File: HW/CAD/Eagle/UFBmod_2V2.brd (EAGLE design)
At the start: 98.4 x 89.5 mm, 204 parts, among them J1411 ABRACON_ARJE-0034, T0551 MMBT2222, U0501 MIDAS_MCCOG21605B6W-FPTLWI, U0601 MAX5217, U0701 AT86RF215-ZU, U0711 ASVTX-13-D-26.000MHZ-I05-T, U0811 PE4259, U0821 RFX1010, U0881 B39871B3440U410, U0911 FT232HL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

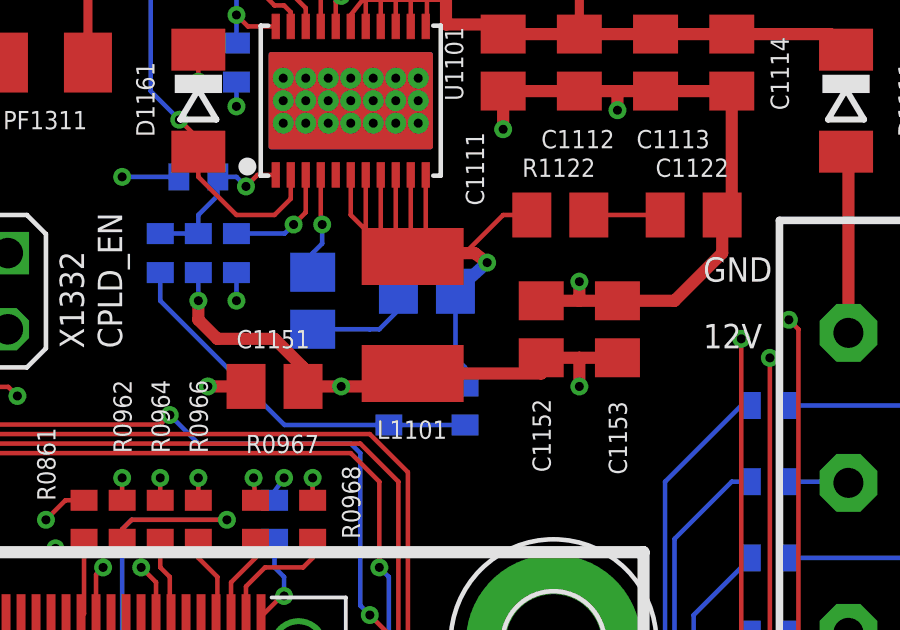
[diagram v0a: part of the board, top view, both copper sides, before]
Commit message: HW - Eagle - V2.2 - inductor sizes fixed
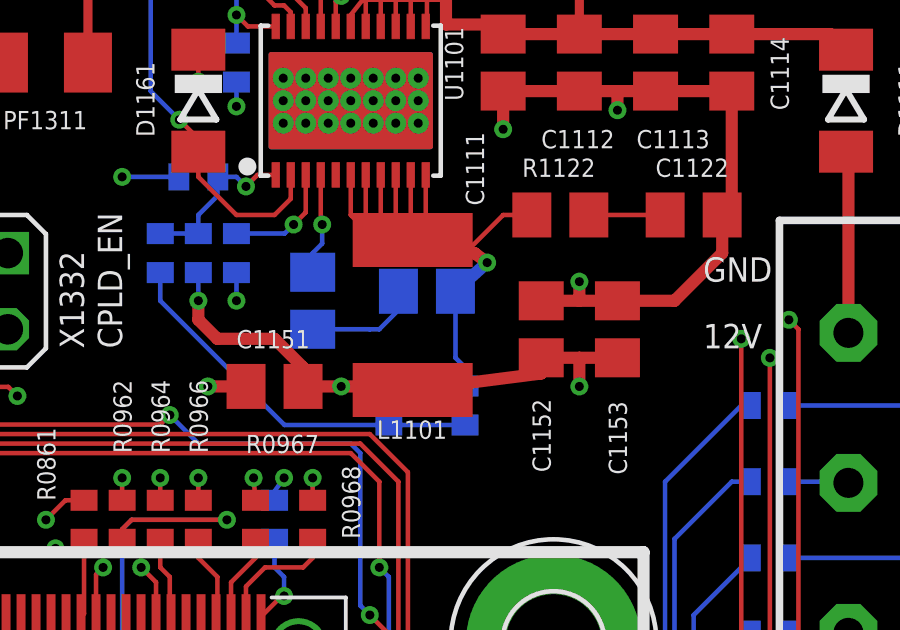
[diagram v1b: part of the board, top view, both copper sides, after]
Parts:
- L1101: value 440nH -> 470nH; device df4iah_rcl:L1812 -> df4iah_rcl:L5650M
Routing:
- net TPS_LL: track 31.4 -> 33.1 mm
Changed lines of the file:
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@@
 <layer number="42" name="bRestrict" color="1" fill="10" visible="yes" active="yes"/>
 <layer number="43" name="vRestrict" color="2" fill="10" visible="yes" active="yes"/>
-<layer number="44" name="Drills" color="7" fill="1" visible="yes" active="yes"/>
+<layer number="44" name="Drills" color="7" fill="1" visible="no" active="yes"/>
 <layer number="45" name="Holes" color="7" fill="1" visible="yes" active="yes"/>
 <layer number="46" name="Milling" color="3" fill="1" visible="yes" active="yes"/>
-<layer number="47" name="Measures" color="13" fill="1" visible="no" active="yes"/>
+<layer number="47" name="Measures" color="13" fill="1" visible="yes" active="yes"/>
 <layer number="48" name="Document" color="7" fill="1" visible="yes" active="yes"/>
 <layer number="49" name="Reference" color="7" fill="1" visible="yes" active="yes"/>
@@
 <element name="H1512" library="df4iah_holes" package="3,2-PAD" value="MOUNT-PAD-ROUND3.2" x="5.08" y="5.08" locked="yes" smashed="yes"/>
 <element name="H1514" library="df4iah_holes" package="3,2-PAD" value="MOUNT-PAD-ROUND3.2" x="93.345" y="5.08" locked="yes" smashed="yes"/>
-<element name="L1101" library="df4iah_rcl" package="L1812" value="440nH" x="73.18375" y="72.86625" smashed="yes" rot="R90">
+<element name="L1101" library="df4iah_rcl" package="L5650M" value="470nH" x="73.18375" y="72.86625" smashed="yes" rot="R90">
 <attribute name="NAME" x="71.993125" y="68.73875" size="0.6096" layer="25" font="vector" ratio="10"/>
 <attribute name="VALUE" x="75.72375" y="71.59625" size="0.6096" layer="27" font="vector" ratio="10" rot="R90"/>
@@
 <wire x1="77.47" y1="71.44" x2="78.74" y2="71.44" width="0.4064" layer="1"/>
 <wire x1="78.74" y1="71.44" x2="80.01" y2="71.44" width="0.4064" layer="1"/>
-<wire x1="73.18375" y1="70.91625" x2="77.47" y2="70.91625" width="0.4064" layer="1"/>
+<wire x1="73.18375" y1="70.36625" x2="77.47" y2="70.91625" width="0.4064" layer="1"/>
 <wire x1="77.47" y1="70.91625" x2="77.47" y2="71.44" width="0.4064" layer="1"/>
 <wire x1="69.53" y1="70.485" x2="70.8025" y2="70.485" width="0.4064" layer="1"/>
 <wire x1="70.8025" y1="70.485" x2="73.18375" y2="70.485" width="0.4064" layer="1"/>
-<wire x1="73.18375" y1="70.485" x2="73.18375" y2="70.91625" width="0.4064" layer="1"/>
+<wire x1="73.18375" y1="70.485" x2="73.18375" y2="70.36625" width="0.4064" layer="1"/>
 <via x="78.74" y="70.485" extent="1-16" drill="0.3"/>
 <wire x1="78.74" y1="70.485" x2="78.74" y2="71.44" width="0.4064" layer="1"/>
@@
 <wire x1="71.12" y1="77.535" x2="71.12" y2="76.2" width="0.1524" layer="1"/>
 <wire x1="71.12" y1="76.2" x2="72.50375" y2="74.81625" width="0.1524" layer="1"/>
-<wire x1="72.50375" y1="74.81625" x2="73.18375" y2="74.81625" width="0.1524" layer="1"/>
+<wire x1="72.50375" y1="74.81625" x2="73.18375" y2="75.36625" width="0.1524" layer="1"/>
 <wire x1="71.62" y1="77.535" x2="71.62" y2="74.81625" width="0.1524" layer="1"/>
-<wire x1="71.62" y1="74.81625" x2="73.18375" y2="74.81625" width="0.1524" layer="1"/>
+<wire x1="71.62" y1="74.81625" x2="73.18375" y2="75.36625" width="0.1524" layer="1"/>
 <wire x1="72.12" y1="77.535" x2="72.12" y2="74.81625" width="0.1524" layer="1"/>
-<wire x1="72.12" y1="74.81625" x2="73.18375" y2="74.81625" width="0.1524" layer="1"/>
+<wire x1="72.12" y1="74.81625" x2="73.18375" y2="75.36625" width="0.1524" layer="1"/>
 <wire x1="72.62" y1="77.535" x2="72.62" y2="74.81625" width="0.1524" layer="1"/>
-<wire x1="72.62" y1="74.81625" x2="73.18375" y2="74.81625" width="0.1524" layer="1"/>
+<wire x1="72.62" y1="74.81625" x2="73.18375" y2="75.36625" width="0.1524" layer="1"/>
 <wire x1="73.12" y1="77.535" x2="73.12" y2="74.81625" width="0.1524" layer="1"/>
-<wire x1="73.12" y1="74.81625" x2="73.18375" y2="74.81625" width="0.1524" layer="1"/>
+<wire x1="73.12" y1="74.81625" x2="73.18375" y2="75.36625" width="0.1524" layer="1"/>
 <wire x1="73.62" y1="77.535" x2="73.62" y2="74.81625" width="0.1524" layer="1"/>
-<wire x1="73.62" y1="74.81625" x2="73.18375" y2="74.81625" width="0.1524" layer="1"/>
+<wire x1="73.62" y1="74.81625" x2="73.18375" y2="75.36625" width="0.1524" layer="1"/>
 <wire x1="77.155" y1="76.2" x2="76.2" y2="76.2" width="0.1524" layer="1"/>
 <wire x1="76.2" y1="76.2" x2="74.93" y2="74.93" width="0.1524" layer="1"/>
 <wire x1="74.93" y1="74.93" x2="73.2975" y2="74.93" width="0.4064" layer="1"/>
-<wire x1="73.2975" y1="74.93" x2="73.18375" y2="74.81625" width="0.4064" layer="1"/>
+<wire x1="73.2975" y1="74.93" x2="73.18375" y2="75.36625" width="0.4064" layer="1"/>
 <via x="75.6666" y="74.6125" extent="1-16" drill="0.3"/>
 <wire x1="74.93" y1="74.93" x2="75.2475" y2="74.93" width="0.4064" layer="1"/>
